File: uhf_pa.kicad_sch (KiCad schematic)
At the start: 26 parts, among them U12 TPS22950_Q1, U13 TQP7M9106

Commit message: Change MFT number for R31
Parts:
- R31: JLCPCB Part # C4176290 -> C169259; Manufacturer_Part_Number ERJ-H3EF1103V -> ERJ-3EKF4700V
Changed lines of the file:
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@@
       (effects (font (size 1.27 1.27)) hide)
     )
-    (property "JLCPCB Part #" "C4176290" (id 7) (at 152.4 59.69 0)
+    (property "JLCPCB Part #" "C169259" (id 7) (at 152.4 59.69 0)
       (effects (font (size 1.27 1.27)) hide)
     )
-    (property "Manufacturer_Part_Number" "ERJ-H3EF1103V" (id 8) (at 152.4 59.69 0)
+    (property "Manufacturer_Part_Number" "ERJ-3EKF4700V" (id 8) (at 152.4 59.69 0)
       (effects (font (size 1.27 1.27)) hide)
     )

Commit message: Fix bug with footprints of components for R27 and R28: 0402->0603, replace manufacter number and JLCPCB part id.
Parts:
- R27: JLCPCB Part # C843898 -> C25221; Manufacturer_Part_Number CRCW0402240RFKEDC -> 0603WAJ0241T5E
- R28: JLCPCB Part # C273692 -> C482820; Manufacturer_Part_Number RC0402FR-07280RL -> RC0603FR-07280RL
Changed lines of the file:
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@@
       (effects (font (size 1.27 1.27)) hide)
     )
-    (property "JLCPCB Part #" "C273692" (id 7) (at 115.57 96.52 0)
+    (property "JLCPCB Part #" "C482820" (id 7) (at 115.57 96.52 0)
       (effects (font (size 1.27 1.27)) hide)
     )
-    (property "Manufacturer_Part_Number" "RC0402FR-07280RL " (id 8) (at 115.57 96.52 0)
+    (property "Manufacturer_Part_Number" "RC0603FR-07280RL" (id 8) (at 115.57 96.52 0)
       (effects (font (size 1.27 1.27)) hide)
     )
@@
       (effects (font (size 1.27 1.27)) hide)
     )
-    (property "JLCPCB Part #" "C843898" (id 7) (at 107.95 96.52 0)
+    (property "JLCPCB Part #" "C25221" (id 7) (at 107.95 96.52 0)
       (effects (font (size 1.27 1.27)) hide)
     )
-    (property "Manufacturer_Part_Number" "CRCW0402240RFKEDC " (id 8) (at 107.95 96.52 0)
+    (property "Manufacturer_Part_Number" "0603WAJ0241T5E" (id 8) (at 107.95 96.52 0)
       (effects (font (size 1.27 1.27)) hide)
     )

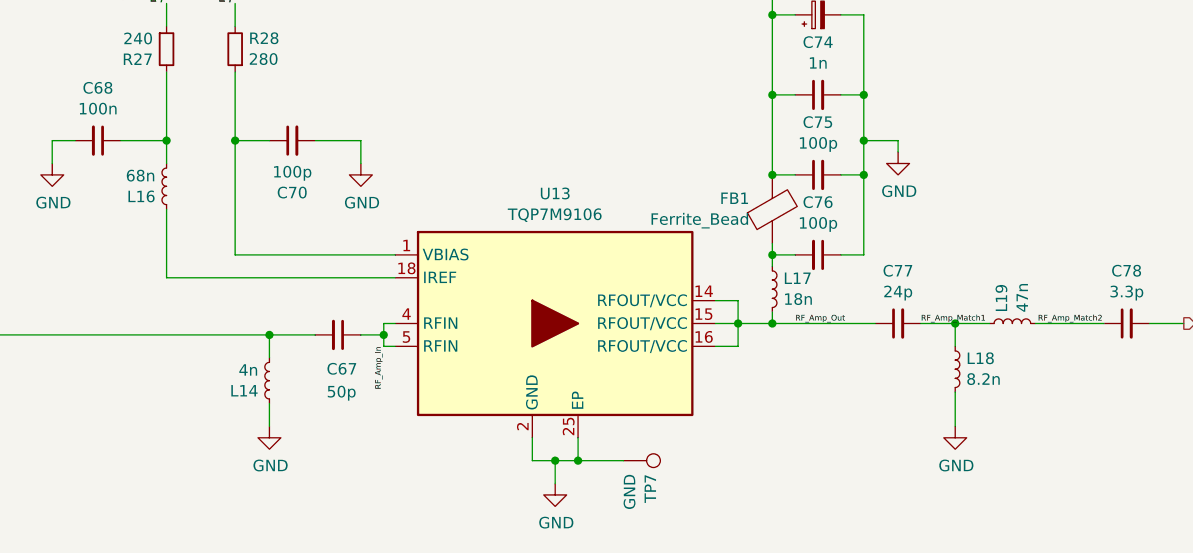
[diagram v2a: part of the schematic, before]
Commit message: Update kicad files to v9.0 from v6.0
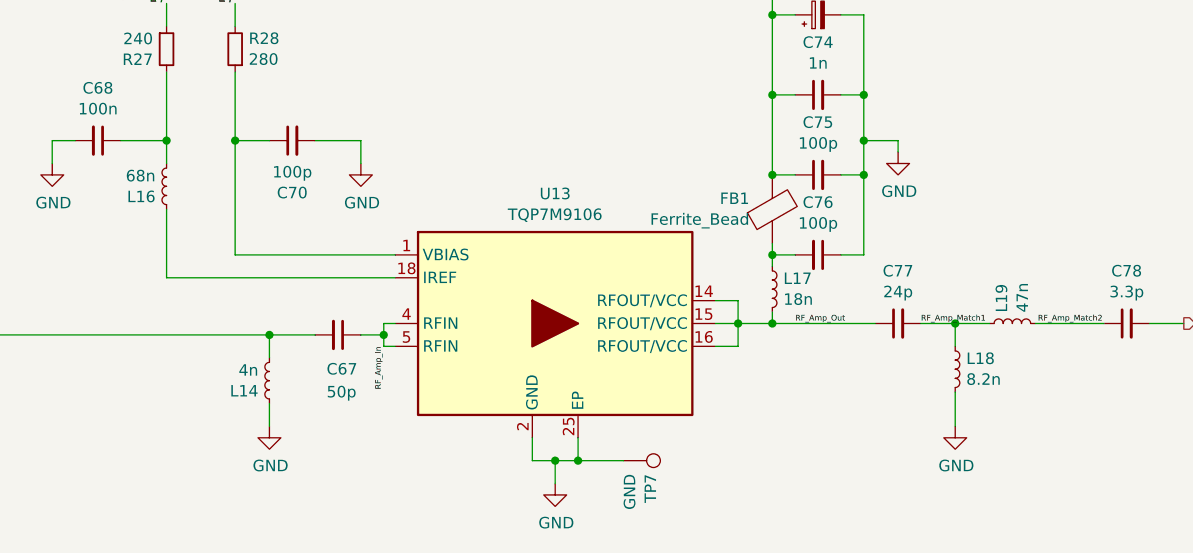
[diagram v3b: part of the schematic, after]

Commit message: Tweak RF amplifier settings: C77 from 24pF to 33pF, L18 from 8.2nH to 5.6nH
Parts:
- C77: value 24p -> 33p; JLCPCB Part # C3833393 -> C70465; Manufacturer_Part_Number UMK105CG240JV-F -> CL05C330JB5NNNC; Mnf. AVX -> (none); PartNumber 04025U240FAT2A -> (none)
- L18: value 8.2n -> 5.6n; JLCPCB Part # C341788 -> (none); Manufacturer_Part_Number LQW15AN8N2H00D -> LQW15AN5N6C1ZD; PartNumber LQW15AN8N2H00D -> LQW15AN5N6C1ZD
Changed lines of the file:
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@@
 			)
 		)
-		(property "Value" "24p"
+		(property "Value" "33p"
 			(at 189.23 123.4948 90)
 			(effects
@@
 			)
 		)
-		(property "Mnf." "AVX"
+		(property "JLCPCB Part #" "C70465"
 			(at 189.23 127 0)
 			(effects
@@
 			)
 		)
-		(property "PartNumber" "04025U240FAT2A"
-			(at 189.23 127 0)
-			(effects
-				(font
-					(size 1.27 1.27)
-				)
-				(hide yes)
-			)
-		)
-		(property "JLCPCB Part #" "C3833393"
-			(at 189.23 127 0)
-			(effects
-				(font
-					(size 1.27 1.27)
-				)
-				(hide yes)
-			)
-		)
-		(property "Manufacturer_Part_Number" "UMK105CG240JV-F"
+		(property "Manufacturer_Part_Number" "CL05C330JB5NNNC"
 			(at 189.23 127 0)
 			(effects
@@
 			)
 		)
-		(property "Value" "8.2n"
+		(property "Value" "5.6n"
 			(at 196.7992 133.223 0)
 			(effects
@@
 			)
 		)
-		(property "PartNumber" "LQW15AN8N2H00D"
+		(property "PartNumber" "LQW15AN5N6C1ZD"
 			(at 195.58 132.08 0)
 			(effects
@@
 			)
 		)
-		(property "JLCPCB Part #" "C341788"
+		(property "JLCPCB Part #" ""
 			(at 195.58 132.08 0)
 			(effects
@@
 			)
 		)
-		(property "Manufacturer_Part_Number" "LQW15AN8N2H00D "
+		(property "Manufacturer_Part_Number" "LQW15AN5N6C1ZD"
 			(at 195.58 132.08 0)
 			(effects
